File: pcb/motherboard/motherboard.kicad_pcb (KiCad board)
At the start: 4 copper layers, 73.7 x 76.2 mm, 88 parts, among them J1 749801122R, J10 HEADER-2x05, J11 Standoff, J12 Standoff, J13 DOUT, J14 VOUT-R, J15 GND, J2 DISPLAY, J3 BARREL_JACK, J4 Micro_SD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

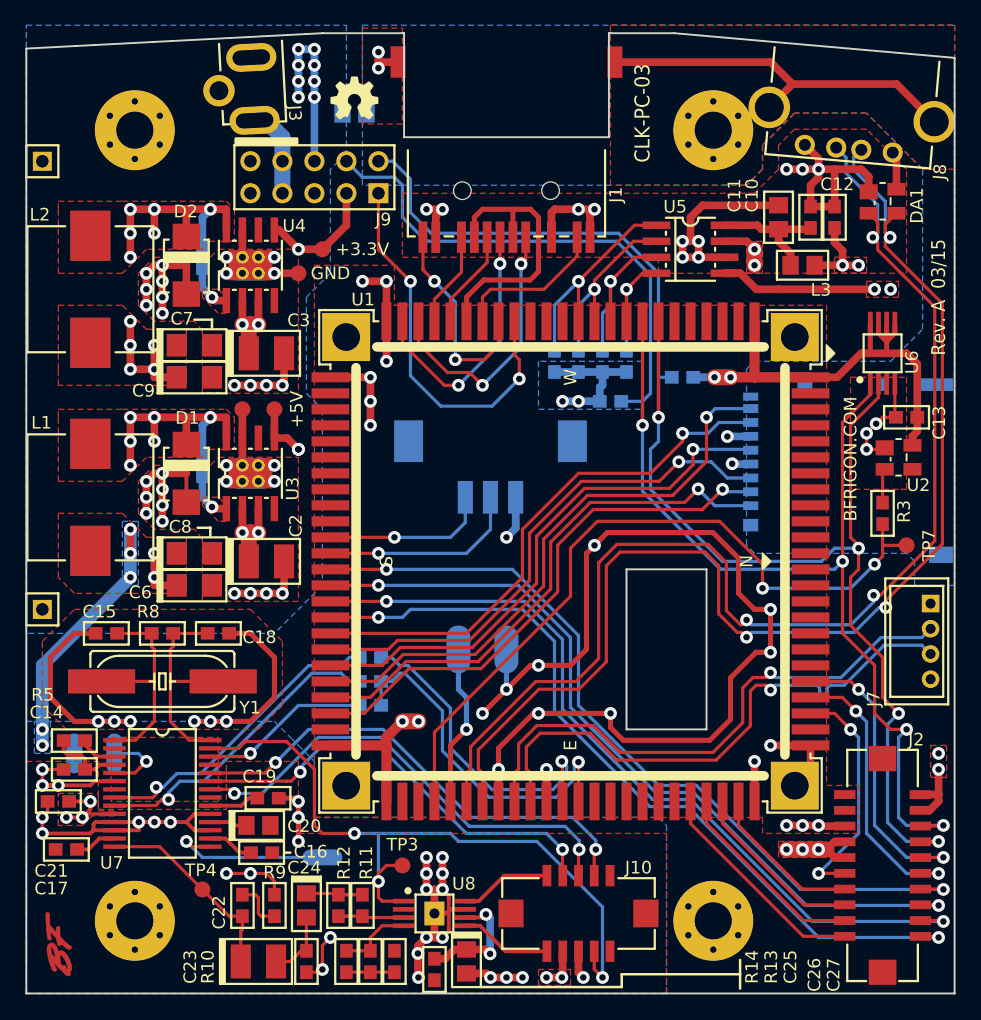
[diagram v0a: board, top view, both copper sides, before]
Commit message: Changed crystal location for PCM2704
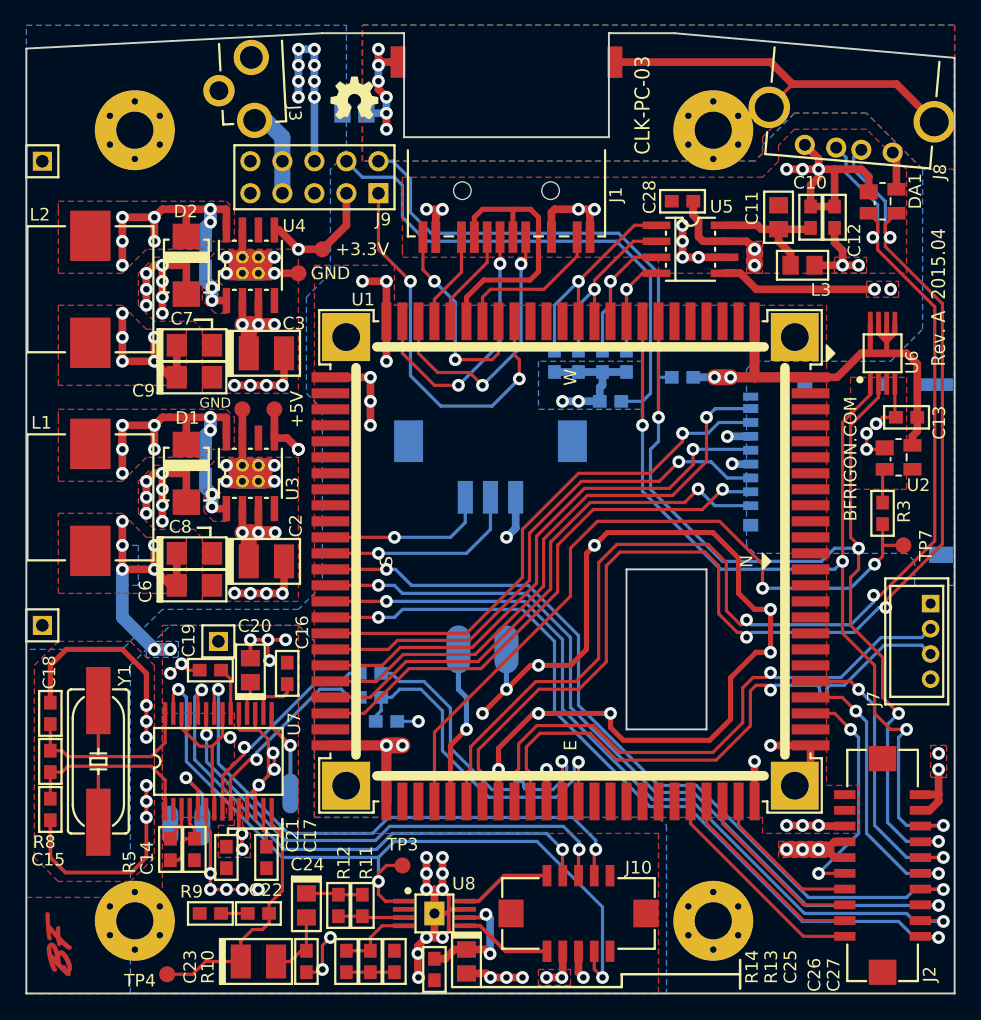
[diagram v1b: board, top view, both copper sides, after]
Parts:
- added C28: 100nF, SMT:C-0603, F.Cu at (153.7, 89.5)
- added J16: Standoff, Conn-Header:HDR-M-1x01, F.Cu at (116.8, 124.5)
- added REF**: Val**, Symbols:Gauge-X-100mm, B.Cu at (88.9, 152.4)
- added REF**: Val**, Symbols:Gauge-X-100mm, F.Cu at (101.6, 165.1)
- H1, H2, H3, H4: footprint Misc:Hole-Screw-#4 -> Conn-Wire-Pads:Hole-Screw-#4
- J1: value 749801122R -> 7498011122R
- J3: value BARREL_JACK -> PJ-013C; footprint Conn-IO:CUI-PJ-013C -> Conn-Power:CUI-PJ-031CH
- J4: value Micro_SD -> DM3AT-SF-PEJM5
- TP3: value TEST-POINT -> DAC_SHDN
- U3: value ADP2302 -> ADP2302ARDZ-5.0
- U4: value ADP2302 -> ADP2303ARDZ-3.3
- U5: value LM3526M-L -> LM3526M-H
- moved C17 15.9 mm to (120.7, 141.6), turned to 90 degrees
- moved C18 14.8 mm to (103.5, 130.2), turned to 270 degrees
- moved C15 14.7 mm to (103.5, 137.8), turned to 270 degrees
- moved C16 14.4 mm to (122.3, 127.0), turned to 270 degrees
- moved C21 14.1 mm to (117.5, 141.6), turned to 90 degrees
- moved R8 13.5 mm to (103.5, 134.0), turned to 90 degrees
- moved C20 12.3 mm to (119.4, 126.7), turned to 90 degrees
- moved R5 11.5 mm to (113.0, 141.0), turned to 90 degrees
- moved C14 11.4 mm to (114.9, 141.0), turned to 90 degrees
- moved C19 11.1 mm to (116.2, 126.7), turned to 0 degrees
- moved J15 9.53 mm to (113.0, 139.1)
- moved J13 9.03 mm to (115.6, 139.1)
- moved Y1 8.13 mm to (107.3, 134.0), turned to 90 degrees
- moved TP4 7.29 mm to (112.8, 150.9)
- moved J14 5.68 mm to (122.6, 136.5), turned to 180 degrees
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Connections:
- net Net-(J5-Pad1) renamed +BATT
- C1 pad 1: Net-(C1-Pad1) -> GNDPWR
- J10 pad 4: /Audio/HID2 -> /Audio/HID0
- J10 pad 6: /Audio/HID0 -> /Audio/HID1
- J10 pad 8: /Audio/HID1 -> /Audio/HID2
- J2 pad 13: /SPI-CS0 -> /SPI-MISO
- J2 pad 15: /SPI-CLK -> /SPI-MOSI
- J2 pad 17: /SPI-MOSI -> /SPI-CLK
- J2 pad 19: /SPI-MISO -> /SPI-CS0
- U1 pad S10: /SPI-MOSI -> /SPI-CLK
- U1 pad S11: /SPI-CLK -> /SPI-MOSI
- U1 pad S12: /SPI-CS0 -> /SPI-MISO
- U1 pad S9: /SPI-MISO -> /SPI-CS0
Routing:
- net GND: track 351.5 -> 318.8 mm, vias 110 -> 108
- net /Audio/DAC_VDD: track 19.6 -> 37.4 mm, vias 1 -> 2
- net (no net): track 0.00 -> 16.6 mm, vias 0 -> 3
- net /Audio/USB+: track 24.4 -> 16.2 mm
- net GNDPWR: track 32.2 -> 39.7 mm, vias 2 -> 6
- net /Audio/USB-: track 24.4 -> 17.2 mm
- net /Audio/HID0: track 37.4 -> 44.3 mm
- net /Audio/VOUT-R: track 13.4 -> 6.96 mm
- net +3V3: track 164.5 -> 158.5 mm
- net /Audio/DAC_SHDN: track 57.3 -> 62.8 mm
- net +5V: track 195.0 -> 189.6 mm, vias 20 -> 19
- net /Audio/HID1: track 34.8 -> 39.7 mm
- net /Audio/HID2: track 38.5 -> 43.0 mm
- net /Audio/VOUT-L: track 16.1 -> 20.5 mm
- net /PSU/SW_5V: track 20.4 -> 22.3 mm, vias 6 -> 7
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- added copper zone on 3.Power, net +9V
- added copper zone on 2.GND, net GNDPWR
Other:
- rule pad_to_mask_clearance: 0.1016 -> 0.127
- board text added: "Rev. A 2015.04"
- board text removed: "Rev. A 03/15"

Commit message: Tidy up motherboard schematic
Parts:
- C2, C3: value 10uF (25v) -> 100uF (16v)
- C22: value 0.022uF 10V -> 0.022uF (10V)
- C23, C24: value 100uF 10V -> 100uF (10V)
- C6, C8: value 22uF -> 47uF (10v)
- C7, C9: value 47uF -> 47uF 6.3v
- DA1: value SR05 -> CD143A-SR05
- J10: value HEADER-2x05 -> DF13A-10DP-1.25V
- J11, J12, J16: value Standoff -> 103741-1
- J2: value DISPLAY -> DF13A-20DP-1.25V(25)
- J6: value DEBUG -> DF3DZ-3P-2V21
- J7: value HEADER-1x04 -> DF3A-4P-2DSA
- J8: value USB-A -> 292303-1
- J9: value AUX PWR -> 103777-5
- L1, L2: value 10uH -> 4.3uH
- L3: value INDUCTOR -> 1A
- U2: value CAT811 -> CAT811TTBI-T3
- Y1: value CRYSTAL -> 12.00 Mhz

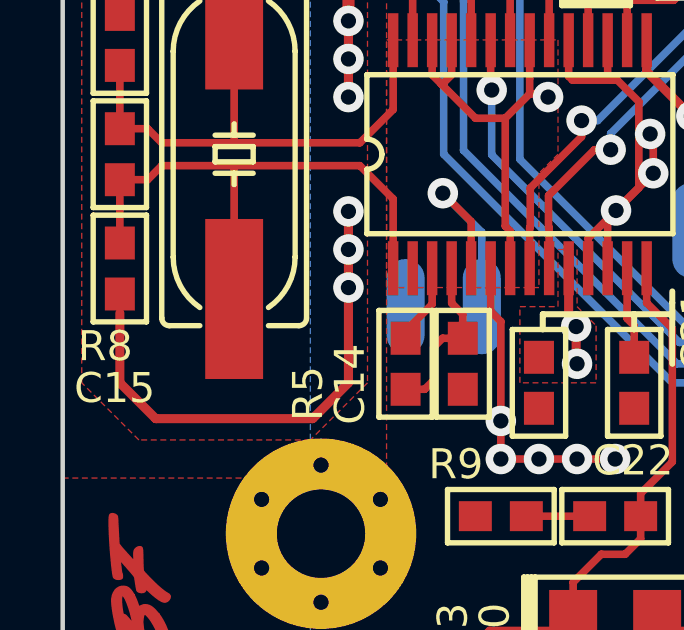
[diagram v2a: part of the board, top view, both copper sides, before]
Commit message: Added 3D views of PC-03 and PC04
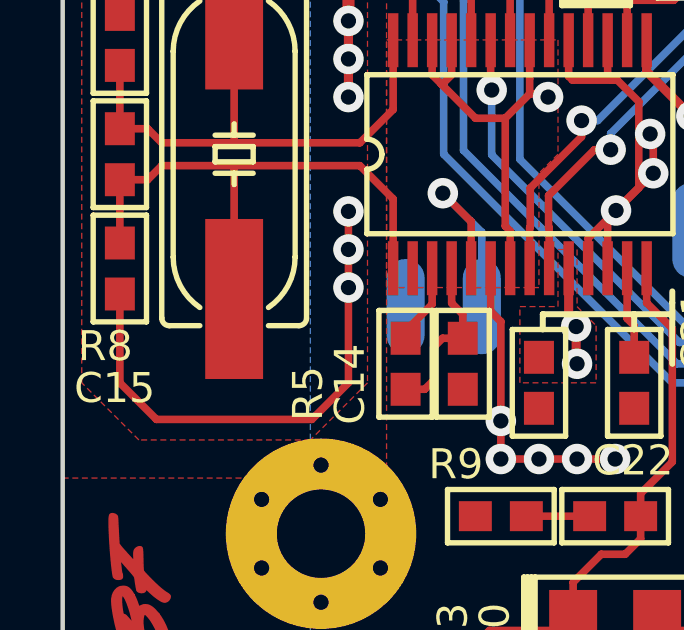
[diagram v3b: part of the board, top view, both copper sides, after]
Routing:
- net GND: track 318.8 -> 336.1 mm, vias 108 -> 111
- net (no net): track 16.6 -> 0.00 mm, vias 3 -> 0
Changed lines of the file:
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@@
     (user_trace_width 1.27)
     (trace_clearance 0.3048)
-    (zone_clearance 0.6096)
+    (zone_clearance 0.254)
     (zone_45_only yes)
     (trace_min 0.254)
@@
   (gr_line (start 101.6 152.4) (end 175.26 152.4) (angle 90) (layer Edge.Cuts) (width 0.15))
   (gr_line (start 101.6 152.4) (end 101.6 77.4192) (angle 90) (layer Edge.Cuts) (width 0.15))
-  (segment (start 103.505 139.28) (end 103.505 141.605) (width 0.3048) (layer F.Cu) (net 0) (status 10))
-  (segment (start 104.698799 142.798799) (end 109.931201 142.798799) (width 0.3048) (layer F.Cu) (net 0))
-  (segment (start 103.505 141.605) (end 104.698799 142.798799) (width 0.3048) (layer F.Cu) (net 0))
-  (via (at 111.125 138.43) (size 1.016) (layers F.Cu B.Cu) (net 0))
-  (segment (start 111.125 141.605) (end 111.125 138.43) (width 0.3048) (layer F.Cu) (net 0))
-  (segment (start 109.931201 142.798799) (end 111.125 141.605) (width 0.3048) (layer F.Cu) (net 0))
-  (via (at 111.125 135.89) (size 1.016) (drill 0.508) (layers F.Cu B.Cu) (net 0))
-  (via (at 111.125 137.16) (size 1.016) (drill 0.508) (layers F.Cu B.Cu) (net 0))
-  (segment (start 111.125 138.43) (end 111.125 137.16) (width 0.3048) (layer F.Cu) (net 0))
-  (segment (start 111.125 135.89) (end 111.125 137.16) (width 0.3048) (layer F.Cu) (net 0))
   (segment (start 142.24 90.805) (end 141.605 90.17) (width 0.4064) (layer F.Cu) (net 1))
   (segment (start 141.605 90.17) (end 140.335 90.17) (width 0.4064) (layer F.Cu) (net 1))
@@
   (segment (start 153.67 91.44) (end 153.67 92.71) (width 0.6096) (layer F.Cu) (net 2))
   (segment (start 114.3 113.411) (end 114.3 111.125) (width 0.6096) (layer F.Cu) (net 2) (status 10))
-  (via (at 111.125 132.08) (size 1.016) (drill 0.508) (layers F.Cu B.Cu) (net 2))
+  (via (at 111.125 132.08) (size 1.016) (layers F.Cu B.Cu) (net 2))
   (segment (start 111.125 129.54) (end 111.125 130.81) (width 0.3048) (layer F.Cu) (net 2))
-  (via (at 111.125 130.81) (size 1.016) (drill 0.508) (layers F.Cu B.Cu) (net 2))
+  (via (at 111.125 130.81) (size 1.016) (layers F.Cu B.Cu) (net 2))
   (segment (start 111.125 132.08) (end 111.125 130.81) (width 0.3048) (layer F.Cu) (net 2))
+  (segment (start 103.505 138.645) (end 103.505 141.605) (width 0.254) (layer F.Cu) (net 2))
+  (segment (start 104.724199 142.824199) (end 109.905801 142.824199) (width 0.254) (layer F.Cu) (net 2))
+  (segment (start 103.505 141.605) (end 104.724199 142.824199) (width 0.254) (layer F.Cu) (net 2))
+  (via (at 111.125 138.43) (size 1.016) (layers F.Cu B.Cu) (net 2))
+  (segment (start 111.125 141.605) (end 111.125 138.43) (width 0.254) (layer F.Cu) (net 2))
+  (segment (start 109.905801 142.824199) (end 111.125 141.605) (width 0.254) (layer F.Cu) (net 2))
+  (via (at 111.125 137.16) (size 1.016) (layers F.Cu B.Cu) (net 2))
+  (segment (start 111.125 138.43) (end 111.125 137.16) (width 0.254) (layer F.Cu) (net 2))
+  (via (at 111.125 135.89) (size 1.016) (layers F.Cu B.Cu) (net 2))
+  (segment (start 111.125 137.16) (end 111.125 135.89) (width 0.254) (layer F.Cu) (net 2))
   (segment (start 138.43 96.52) (end 137.795 97.155) (width 0.254) (layer F.Cu) (net 3))
   (segment (start 137.795 97.155) (end 137.795 99.06) (width 0.254) (layer F.Cu) (net 3) (status 20))
@@
   (segment (start 116.351295 136.378705) (end 116.515 136.54241) (width 0.254) (layer F.Cu) (net 113))
   (segment (start 116.351295 132.785851) (end 116.351295 136.378705) (width 0.254) (layer F.Cu) (net 113))
-  (via (at 117.77981 132.08) (size 1.016) (drill 0.508) (layers F.Cu B.Cu) (net 113))
+  (via (at 117.77981 132.08) (size 1.016) (layers F.Cu B.Cu) (net 113))
   (segment (start 119.04981 130.81) (end 132.715 130.81) (width 0.3048) (layer 3.Power) (net 113))
   (segment (start 117.77981 132.08) (end 119.04981 130.81) (width 0.3048) (layer 3.Power) (net 113))

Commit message: Wrong polarity on battery connector label
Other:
- board text added: "VBAT - +"
- board text removed: "VBAT + -"
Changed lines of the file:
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@@
   )
   (layers
-    (0 F.Cu signal hide)
+    (0 F.Cu signal)
     (1 2.GND power hide)
     (2 3.Power power hide)
@@
     (effects (font (size 1.1 1.1) (thickness 0.18)) (justify mirror))
   )
-  (gr_text "VBAT\n+  -" (at 137.795 120.65) (layer B.SilkS)
+  (gr_text "VBAT\n-  +" (at 137.795 120.65) (layer B.SilkS)
     (effects (font (size 1.1 1.1) (thickness 0.18)) (justify mirror))
   )
@@
     (polygon
       (pts
-        (xy 110.49 120.015) (xy 109.22 120.015) (xy 109.22 116.84) (xy 110.49 116.84)
+        (xy 109.855 119.38) (xy 108.585 119.38) (xy 108.585 116.205) (xy 109.855 116.205)
       )
     )
